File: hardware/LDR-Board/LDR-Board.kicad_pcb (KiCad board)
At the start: 2 copper layers, 29.2 x 40.6 mm, 6 parts, among them J1 TO SOLAR SHIELD

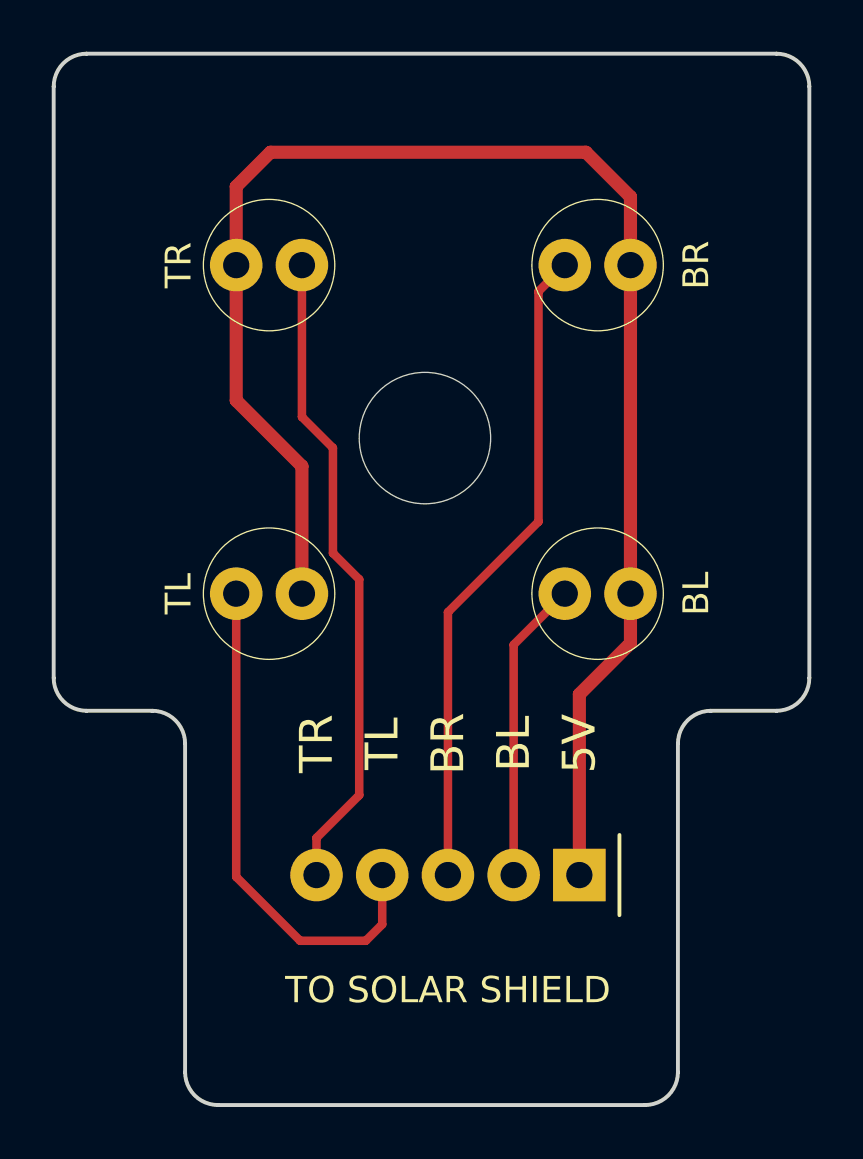
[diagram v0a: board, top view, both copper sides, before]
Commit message: LDR Board v1.2 has two screw holes.
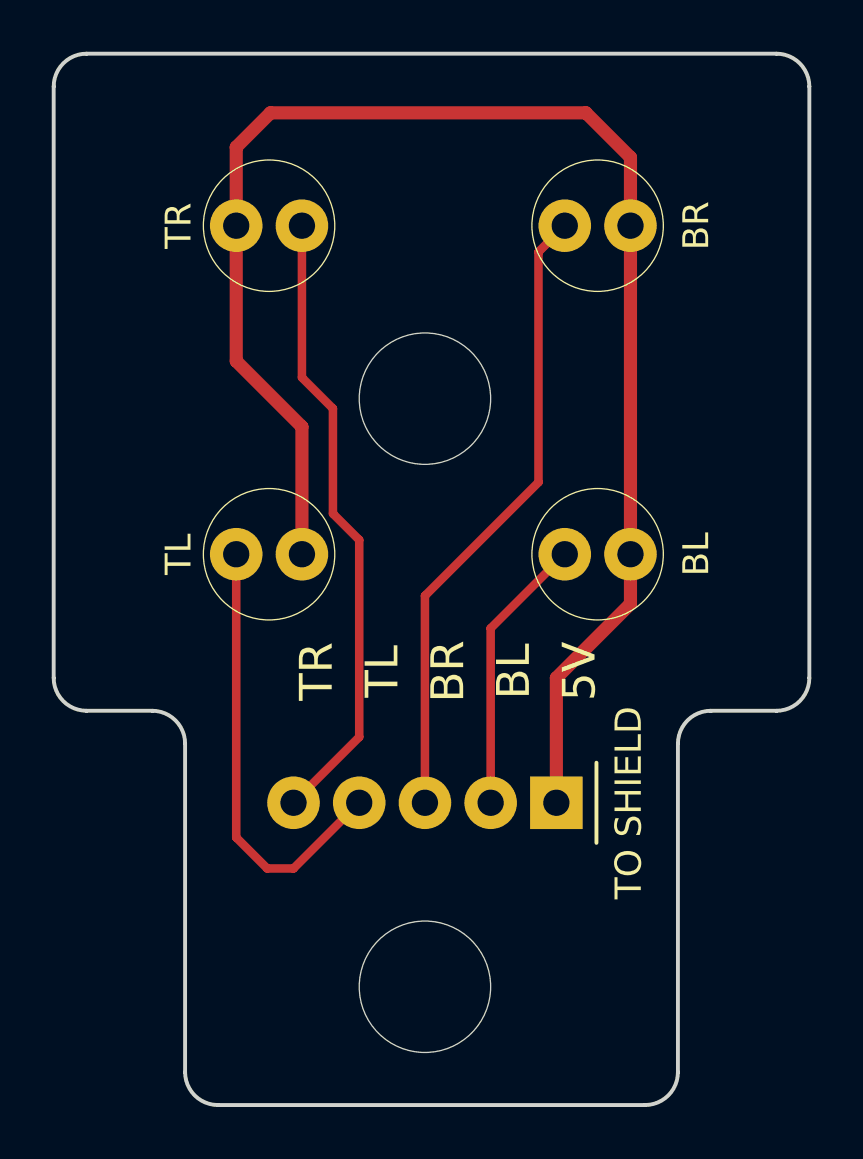
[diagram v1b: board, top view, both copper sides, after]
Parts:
- added V: HOLE-PLATED-200MIL, Wickerlib:HOLE-UNPLATED-200MIL, F.Cu at (19.1, 87.9)
- moved J1 2.93 mm to (24.1, 80.8)
- moved R2 1.52 mm to (25.7, 58.5)
- moved R4 1.52 mm to (13.0, 58.5)
- moved V 1.52 mm to (19.1, 65.2)
- moved R1 1.52 mm to (25.7, 71.2)
- moved R3 1.52 mm to (13.0, 71.2)
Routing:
- net /TOPLEFT: track 19.8 -> 17.3 mm
- net /BOTTOMLEFT: track 11.7 -> 10.8 mm
- net /TOPRIGHT: track 25.2 -> 24.3 mm
- net /BOTTOMRIGHT: track 25.4 -> 24.5 mm
- net +5V: track 60.3 -> 59.4 mm
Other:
- board text added: "LDR Board v1.2"
- board text removed: "LDR Board v1.1"
